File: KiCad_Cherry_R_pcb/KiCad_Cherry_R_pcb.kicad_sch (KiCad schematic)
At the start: 63 parts, among them J1 AudioJack3_SwitchTR, SW1 Esc, SW10 E, SW11 R, SW12 T, SW13 Ctrl, SW14 A, SW15 S, SW16 D, SW17 F, SW18 G, SW19 Shift, SW2 1, SW20 Z, SW21 X, SW22 C, SW23 V, SW24 6, SW25 Fn, SW26 Alt, SW27 Win, SW28 NoConv, SW29 Space, SW3 2, SW4 3, SW5 4, SW6 5, SW7 Tab, SW8 Q, SW9 W, U1 Sparkfun_Pro_Micro

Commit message: feat: Rightの配置が完了
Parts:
- added D14, D21, D28, D34, D35, D36, D37, D38, D39, D40, D41, D42, D7: 1N4148W, Diode_SMD:D_SOD-323, symbol Diode:1N4148W
- added SW14: ], KBD_BrownSugar:CherryMX_Hotswap_via_1U, symbol Switch:SW_Push
- added SW21: \, KBD_BrownSugar:CherryMX_Hotswap_via_1U, symbol Switch:SW_Push
- added SW28: Shift, KBD_BrownSugar:CherryMX_Hotswap_via_1.75U, symbol Switch:SW_Push
- added SW34: ↑, KBD_BrownSugar:CherryMX_Hotswap_via_1U, symbol Switch:SW_Push
- added SW35: ↓, KBD_BrownSugar:CherryMX_Hotswap_via_1U, symbol Switch:SW_Push
- added SW36: BS, KBD_BrownSugar:CherryMX_Hotswap_via_1U, symbol Switch:SW_Push
- added SW37: Enter, KBD_BrownSugar:CherryMX_Hotswap_via_ISO_Enter, symbol Switch:SW_Push
- added SW38: Home, KBD_BrownSugar:CherryMX_Hotswap_via_1U, symbol Switch:SW_Push
- added SW39: End, KBD_BrownSugar:CherryMX_Hotswap_via_1U, symbol Switch:SW_Push
- added SW40: →, KBD_BrownSugar:CherryMX_Hotswap_via_1U, symbol Switch:SW_Push
- added SW41: Free, KBD_BrownSugar:CherryMX_Hotswap_via_1U, symbol Switch:SW_Push
- added SW42: PrtSc, KBD_BrownSugar:CherryMX_Hotswap_via_1U, symbol Switch:SW_Push
- added SW7: `, KBD_BrownSugar:CherryMX_Hotswap_via_1U, symbol Switch:SW_Push
- SW1: value Esc -> 7
- SW10: renamed from SW9; value W -> I
- SW11: renamed from SW10; value E -> O
- SW12: renamed from SW11; value R -> P
- SW13: renamed from SW12; value T -> [
- SW15: renamed from SW13; value Ctrl -> H; footprint KBD_BrownSugar:CherryMX_Hotswap_via_1.75U -> KBD_BrownSugar:CherryMX_Hotswap_via_1U
- SW16: renamed from SW14; value A -> J
- SW17: renamed from SW15; value S -> K
- SW18: renamed from SW16; value D -> L
- SW19: renamed from SW17; value F -> ;
- SW2: value 1 -> 8
- SW20: renamed from SW18; value G -> '
- SW22: renamed from SW19; value Shift -> B; footprint KBD_BrownSugar:CherryMX_Hotswap_via_2.25U -> KBD_BrownSugar:CherryMX_Hotswap_via_1U
- SW23: renamed from SW20; value Z -> N
- SW24: renamed from SW21; value X -> M
- SW25: renamed from SW22; value C -> ,
- SW26: renamed from SW23; value V -> .
- SW27: renamed from SW24; value 6 -> /
- SW29: renamed from SW25; value Fn -> Space; footprint KBD_BrownSugar:CherryMX_Hotswap_via_1.25U -> KBD_BrownSugar:CherryMX_Hotswap_via_2U
- SW3: value 2 -> 9
- SW30: renamed from SW26; value Alt -> Conv
- SW32: renamed from SW28; value NoConv -> Fn
- SW33: renamed from SW29; value Space -> ←; footprint KBD_BrownSugar:CherryMX_Hotswap_via_2U -> KBD_BrownSugar:CherryMX_Hotswap_via_1U
- SW4: value 3 -> 0
- SW5: value 4 -> -
- SW6: value 5 -> =
- SW8: renamed from SW7; value Tab -> Y; footprint KBD_BrownSugar:CherryMX_Hotswap_via_1.5U -> KBD_BrownSugar:CherryMX_Hotswap_via_1U
- SW9: renamed from SW8; value Q -> U
- renumbered D9 to D10, D10 to D11, D11 to D12, D12 to D13, D13 to D15, D14 to D16, D15 to D17, D16 to D18, D17 to D19, D18 to D20, D19 to D22, D20 to D23, D21 to D24, D22 to D25, D23 to D26, D24 to D27, D25 to D29, D26 to D30, D27 to D31, D28 to D32, D29 to D33, D30 to D43, D7 to D8, D8 to D9, SW27 to SW31
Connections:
- net +5V: no longer U1.13 (~D10/A10)
- net Col0: now also SW36.1
- net Col1: now also SW37.1
- net Col2: now also SW38.1
- net Col3: now also SW39.1
- net Col4: now also SW40.1
- net Col5: now also SW35.1, SW42.1
- net GND: now also U1.13 (~D10/A10)
- net Row10: now reaches U1.12 (~D9/A9)
- net Row10: now also D36.1 (K), D37.1 (K), D38.1 (K), D39.1 (K), D40.1 (K), D41.1 (K), D42.1 (K)
- net Col6: now reaches U1.14 (D16)
- net Col6: now also SW14.1, SW21.1, SW28.1, SW34.1, SW41.1, SW7.1
- net Row0 renamed Row5
- net Row5: now also D7.1 (K)
- net Row1 renamed Row6
- net Row6: now also D14.1 (K)
- net Row2 renamed Row7
- net Row7: now also D21.1 (K)
- net Row3 renamed Row8
- net Row8: now also D28.1 (K)
- net Row4 renamed Row9
- net Row9: now also D34.1 (K), D35.1 (K)
- new net: D21.2 (A), SW21.2
- new net: D38.2 (A), SW38.2
- new net: D14.2 (A), SW14.2
- new net: D39.2 (A), SW39.2
- new net: D36.2 (A), SW36.2
- new net: D42.2 (A), SW42.2
- new net: D35.2 (A), SW35.2
- new net: D40.2 (A), SW40.2
- new net: D7.2 (A), SW7.2
- new net: D28.2 (A), SW28.2
- new net: D41.2 (A), SW41.2
- new net: D37.2 (A), SW37.2
- new net: D34.2 (A), SW34.2
- no-connect marks 8 -> 6
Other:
- title: Just the Two of JIS - Left -> Just the Two of JIS - Right
- moved on the sheet: C1, C2, D43, J1, U1

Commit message: feat: Resetピンを追加
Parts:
- added J2: Reset, Connector_PinHeader_1.00mm:PinHeader_1x01_P1.00mm_Vertical, symbol Connector:Conn_01x01_Pin
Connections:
- net at U1.22 (RST): now also J2.1 (Pin_1)
- no-connect marks 6 -> 5
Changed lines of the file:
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@@
 	)
 	(no_connect
-		(at 85.09 194.31)
-	)
-	(no_connect
 		(at 132.08 205.74)
 	)
@@
 					(unit 1)
 				)
+			)
+		)
+	)
+	(symbol
+		(lib_id "Connector:Conn_01x01_Pin")
+		(at 90.17 194.31 0)
+		(mirror y)
+		(unit 1)
+		(exclude_from_sim no)
+		(in_bom yes)
+		(on_board yes)
+		(dnp no)
+		(property "Reference" "J2"
+			(at 96.52 191.77 0)
+			(effects
+				(font
+					(size 1.27 1.27)
+				)
+			)
+		)
+		(property "Value" "Reset"
+			(at 96.52 194.31 0)
+			(effects
+				(font
+					(size 1.27 1.27)
+				)
+			)
+		)
+		(property "Footprint" "Connector_PinHeader_1.00mm:PinHeader_1x01_P1.00mm_Vertical"
+			(at 90.17 194.31 0)
+			(effects
+				(font
+					(size 1.27 1.27)
+				)
+				(hide yes)
+			)
+		)
+		(property "Datasheet" "~"
+			(at 90.17 194.31 0)
+			(effects
+				(font
+					(size 1.27 1.27)
+				)
+				(hide yes)
+			)
+		)
+		(property "Description" "Generic connector, single row, 01x01, script generated"
+			(at 90.17 194.31 0)
+			(effects
+				(font
+					(size 1.27 1.27)
+				)
+				(hide yes)
+			)
+		)
+		(pin "1"
+		)
+		(instances
+			(project "KiCad_Cherry_R_pcb"
+				(path "/63624602-85c8-4a35-8071-08b2ca90618c"
+					(reference "J2")
+					(unit 1)
+				)

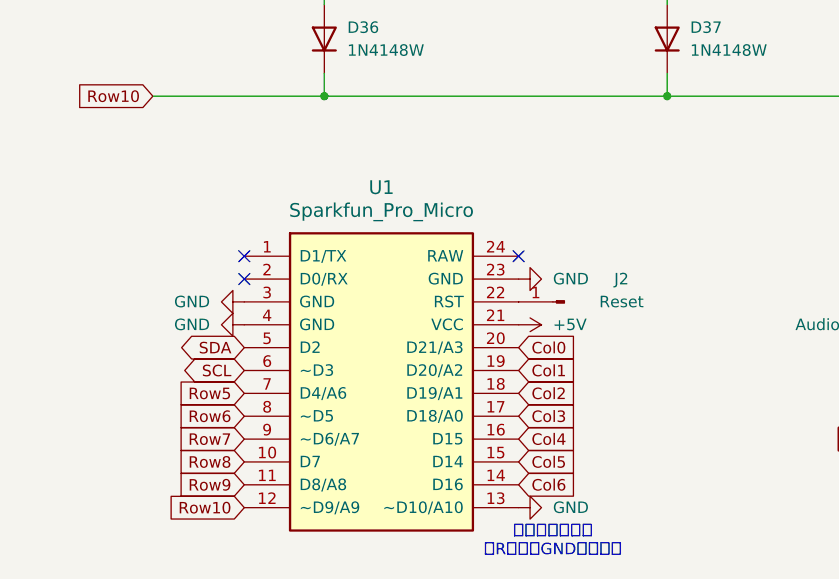
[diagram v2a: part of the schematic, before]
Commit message: feat: Rightのガワを用意
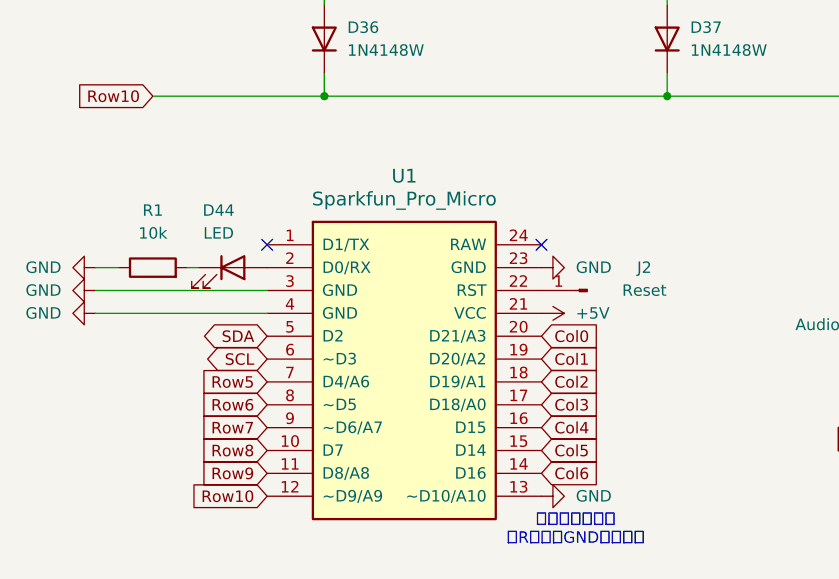
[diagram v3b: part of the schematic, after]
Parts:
- added D44: LED, LED_SMD:LED_0805_2012Metric, symbol Device:LED
- added R1: 10k, Resistor_SMD:R_0805_2012Metric, symbol Device:R
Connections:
- net GND: now also R1.1
- net at U1.2 (D0/RX): now also D44.2 (A)
- new net: D44.1 (K), R1.2
- no-connect marks 5 -> 4
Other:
- moved on the sheet: J2, U1
